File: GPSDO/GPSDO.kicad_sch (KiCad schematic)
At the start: 96 parts, among them IC4 AD8620, IC5 LD1117S12TR_SOT223, IC7 74HC14, IC9 MCP4725, J2 SolderJumper_3_Open, J3 SolderJumper_2_Open, K1 Conn_01x04, K10 Conn_01x03, K11 Conn_01x07, K12 SW_Push, K13 Conn_01x03, K14 Conn_01x05, K2 Conn_01x02, K3 Conn_01x02, K4 Conn_01x03, K5 Jumper_3_Open, K6 Conn_01x05, K7 Conn_01x02, K8 Conn_02x03_Odd_Even, K9 Conn_Coaxial, Q1 NPN

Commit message: changed schematic, OCXO symbol from Gibbi
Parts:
- removed C12: 1µ, symbol Device:C
- removed C15, C5: 100n, symbol Device:C
- removed C16: 1n, symbol Device:C
- removed D3: D, symbol Device:D
- removed F1: 1.6A, symbol Device:Fuse
- removed unit 1 of IC4
- removed IC5: LD1117S12TR_SOT223, Package_TO_SOT_SMD:SOT-223-3_TabPin2, symbol Regulator_Linear:LD1117S12TR_SOT223
- removed IC9: MCP4725, Package_TO_SOT_SMD:SOT-23-6, symbol Analog_DAC:MCP4725xxx-xCH
- removed OCXO1: ~, symbol GPSDO-Components:OCXO
- removed Q1: NPN, symbol Simulation_SPICE:NPN
- removed R14: 10k, symbol Device:R_Potentiometer
- removed R17, R18: 240, symbol Device:R
- removed R19, R20, R21: 2.4k, symbol Device:R
- removed RE1: G6K-2, symbol Relay:G6K-2
- removed TP3: Conn_01x01_Pin, symbol Connector:Conn_01x01_Pin
- added C5: 330n, symbol Device:C_Polarized
- added IC4: AD8620, Package_SO:SOIC-8_3.9x4.9mm_P1.27mm, symbol Amplifier_Operational:AD8620
- added J1: Conn_01x01_Pin, symbol Connector:Conn_01x01_Pin
- added OCXO2: ~, gibbi:OSC5A2B02, symbol GPSDO-Components:OSC5A2B02
- added SW1: SW_Nidec_CAS-120A1, Button_Switch_SMD:Nidec_Copal_CAS-120A, symbol Switch:SW_Nidec_CAS-120A1
- added U1: LM7805_TO220, Package_TO_SOT_THT:TO-220-3_Vertical, symbol Regulator_Linear:LM7805_TO220
- added U2: DAC8571IDGK, Package_SO:MSOP-8_3x3mm_P0.65mm, symbol Analog_DAC:DAC8571IDGK
- C13: value 470µ -> 100n
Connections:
- net GND: now also C5.2, OCXO2.2 (GND), U1.2 (GND), U2.5 (A0), U2.8 (GND)
- net VCC: now also SW1.2 (B)
- net at A1.23 (A4), K14.3 (Pin_3), K6.3 (Pin_3)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: now also U2.7 (SDA)
- net at A1.24 (A5), K14.4 (Pin_4), K6.4 (Pin_4)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: now also U2.6 (SCL)
- net at K7.2 (Pin_2): now also D1.2 (A)
- net at IC4.6 (-): no longer IC4.7
- net at C17.1, C19.1, L3.2: now also OCXO2.5 (VCC)
- net at IC7.1, R22.2, R23.1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: now also OCXO2.1 (10MHz)
- net at C11.2, R15.1: now also IC4.5 (+)
- net at D1.1 (K): now also C5.1, U1.1 (VI); no longer C13.1
- net at R16.1: now also IC4.6 (-), OCXO2.3 (Vcont); no longer A1.22 (A3)
- net at C14.1, L5.1: now also U2.1 (V_{DD}), U2.2 (V_{REF})
- net comp: now reaches A1.15 (D12)
- net comp: now also IC4.7
- net at R16.2: now also U2.3 (V_{SENSE}), U2.4 (V_{OUT})
- net V_ocxo: no longer names the net of A1.20 (A1)
- new net: C13.1, SW1.3 (A), U1.3 (VO)
- new net: J1.1 (Pin_1), SW1.1 (C)
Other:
- note added: "+5V"
- note added: "DC 7 - 25V"
- note removed: "DC 7.5 - 9V"
- note removed: "Manual Holdover"
- note removed: "V_Holdover"
- moved on the sheet: A1, C1, C10, C11, C14, C17, C18, C19, C2, C20, C21, C22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

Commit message: Add Frequency Multiplier and Pico
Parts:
- removed A1: Arduino_Nano_v3, Module:Arduino_Nano, symbol MCU_Module:Arduino_Nano_v3.x
- removed IC4: AD8620, Package_SO:SOIC-8_3.9x4.9mm_P1.27mm, symbol Amplifier_Operational:AD8620
- removed K10, K13, K4: Conn_01x03, symbol Connector_Generic:Conn_01x03
- removed K11: Conn_01x07, symbol Connector_Generic:Conn_01x07
- removed K14, K6: Conn_01x05, symbol Connector_Generic:Conn_01x05
- added C12, C16: 40p, symbol Device:C
- added C15, C23: 0.1u, symbol Device:C
- added J4, J5: SolderJumper_3_Open, symbol Jumper:SolderJumper_3_Open
- added K4, K6: Conn_Coaxial, symbol Connector:Conn_Coaxial
- added R14, R17, R19, R21: 10k, symbol Device:R
- added RV1: 2k, symbol Device:R_Potentiometer
- added RV2: 4k, symbol Device:R_Potentiometer
- added U3: Pico, RPi_Pico:RPi_Pico_SMD_TH, symbol MCU_RaspberryPi_and_Boards:Pico
- added U4, U6: TLV3501AID, Package_SO:SOIC-8_3.9x4.9mm_P1.27mm, symbol Comparator:TLV3501AID
- added U5: 74LVC2G86, symbol 74xGxx:74LVC2G86
- R8: value 2.4k -> 0
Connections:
- net GND: now also C12.1, C16.1, K4.2 (Ext), K6.2 (Ext), R17.2, R19.2, U3.13 (GND), U3.18 (GND), U3.23 (GND), U3.28 (GND), U3.38 (GND), U3.42 (GND), U3.8 (GND), U4.4 (V-), U5.4 (GND), U6.4 (V-)
- net VCC: now also C15.2, R14.1
- net comp: now also U3.29 (GPIO22)
- net at R8.2: now also RV2.1, U5.2
- net at C1.2, C7.1, C8.1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: now also IC1.1 (LD), U3.40 (VBUS); no longer R8.1
- net at K9.1 (In), R24.1, R25.1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: now also R8.1
- net at R12.1, U2.7 (SDA): now also U3.31 (GPIO26_ADC0)
- net at R13.1, U2.6 (SCL): now also U3.32 (GPIO27_ADC1)
- net at R5.1: now also U3.4 (GPIO2)
- net at R7.2: now also J4.1 (A), J5.3 (B)
- net at K1.3 (Pin_3): now also J4.3 (B), J5.1 (A)
- new net: R19.1, R21.2, U6.3 (+)
- new net: C16.2, RV1.2, U6.2 (-)
- new net: C12.2, RV2.2, U4.2 (-)
- new net: R14.2, R17.1, U4.3 (+)
- new net: U4.6, U5.1
- new net: C15.1, U4.7 (V+)
- new net: J4.2 (C), U3.2 (GPIO1)
- new net: C23.1, U6.7 (V+)
- new net: C23.2, R21.1
- new net: J5.2 (C), U3.1 (GPIO0)
- new net: K4.1 (In), U5.3
- new net: U5.5, U6.6
- new net: K6.1 (In), RV1.3, U5.6, U5.7
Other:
- note added: "10MHz out"
- note added: "20MHz out"
- note added: "3.3V or 5V?"
- note added: "40MHz out"
- note removed: "Forced Holdover"
- note removed: "SPI"
- note removed: "Temp Sensor"
- moved on the sheet: C1, C10, C11, C13, C14, C17, C18, C19, C2, C20, C21, C22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

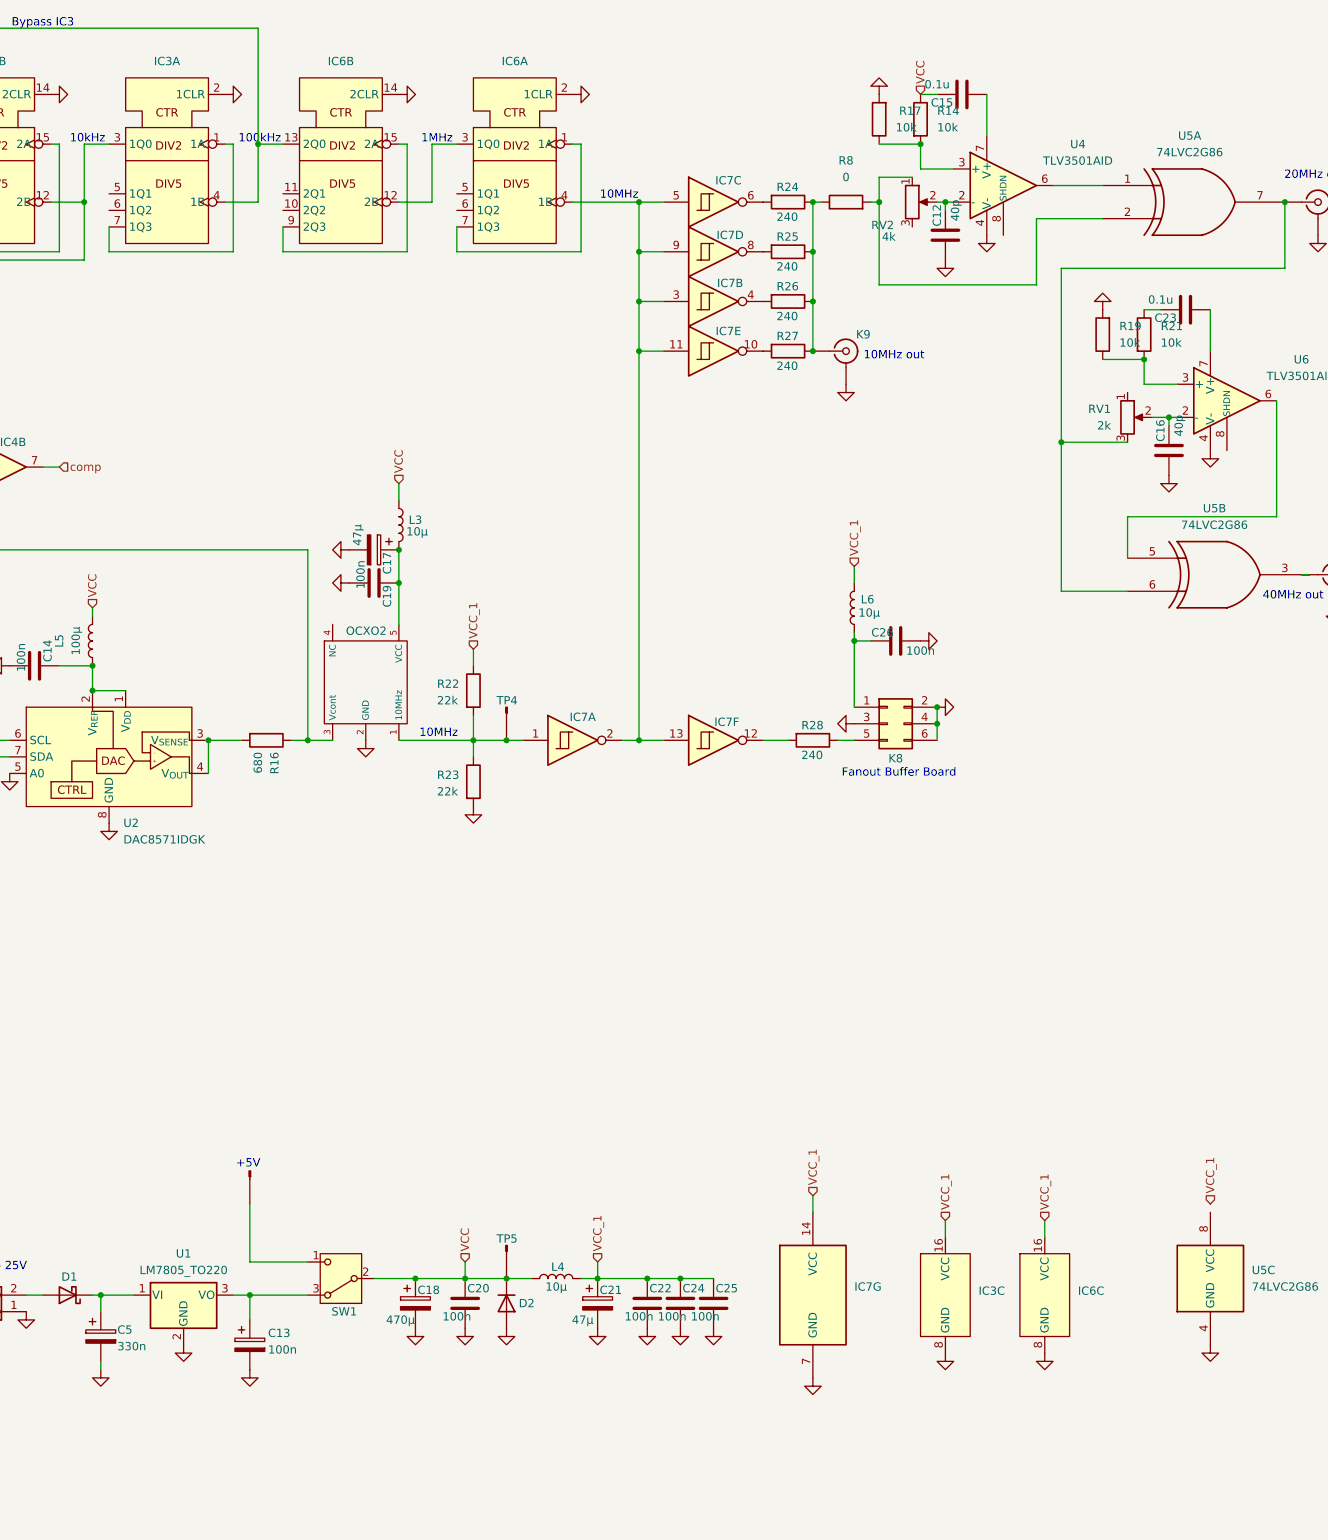
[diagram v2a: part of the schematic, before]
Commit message: minor schematic changes, added most footprints
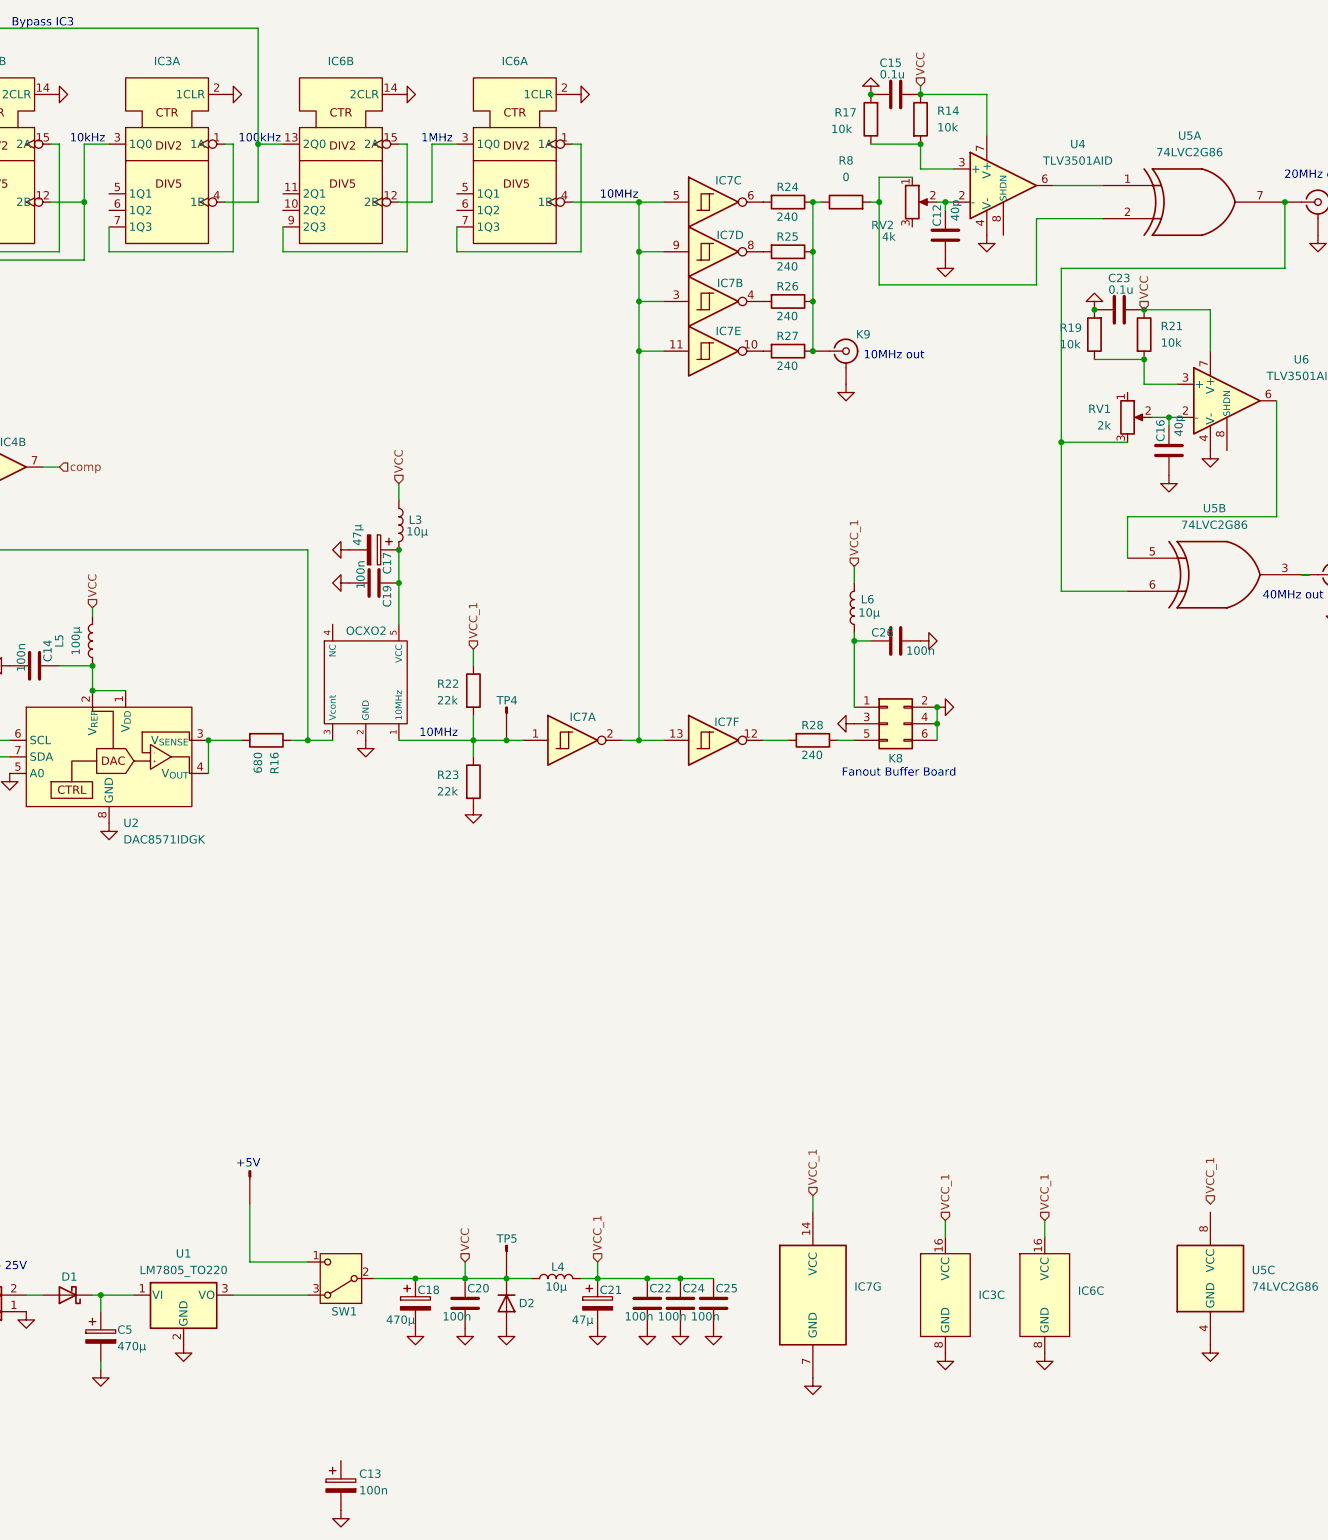
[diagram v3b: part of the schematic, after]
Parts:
- C1, C12, C14, C15, C16, C19, C20, C22, C23, C24, C25, C26, C4, C6, C8: footprint (none) -> Capacitor_SMD:C_1210_3225Metric_Pad1.33x2.70mm_HandSolder
- C10, C9: footprint (none) -> Capacitor_Tantalum_SMD:CP_EIA-7343-43_Kemet-X_Pad2.25x2.55mm_HandSolder
- C11, C3: footprint (none) -> Capacitor_THT:C_Rect_L7.2mm_W3.5mm_P5.00mm_FKS2_FKP2_MKS2_MKP2
- C17, C2, C21, C7: footprint (none) -> Capacitor_THT:CP_Radial_D6.3mm_P2.50mm
- C18: footprint (none) -> Capacitor_THT:CP_Radial_D10.0mm_P5.00mm
- C5: value 330n -> 470µ; footprint (none) -> Capacitor_THT:CP_Radial_D10.0mm_P5.00mm
- D1: footprint Diode_SMD:D_SMA -> Diode_SMD:D_SMA-SMB_Universal_Handsoldering
- D2: footprint (none) -> Diode_THT:D_DO-15_P10.16mm_Horizontal
- IC1, IC3, IC6: footprint (none) -> Package_SO:SOIC-16_3.9x9.9mm_P1.27mm
- J1, TP1, TP2, TP4, TP5: footprint (none) -> TestPoint:TestPoint_Pad_D1.0mm
- J2, J4, J5: footprint (none) -> Jumper:SolderJumper-3_P1.3mm_Open_RoundedPad1.0x1.5mm_NumberLabels
- J3: footprint (none) -> Jumper:SolderJumper-2_P1.3mm_Open_RoundedPad1.0x1.5mm
- K8: footprint (none) -> Connector_IDC:IDC-Header_2x03_P2.54mm_Vertical
- R1, R10, R11, R12, R13, R14, R15, R16, R17, R19, R2, R21, R22, R23, R24, R25, R26, R27, R28, R29, R3, R4, R5, R6, R7, R9: footprint (none) -> Resistor_SMD:R_1210_3225Metric_Pad1.30x2.65mm_HandSolder
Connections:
- net GND: now also C15.2, C23.2
- net VCC: now also C15.1, C23.1, R21.1, U4.7 (V+), U6.7 (V+); no longer C15.2
- net at SW1.3 (A), U1.3 (VO): no longer C13.1
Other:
- moved on the sheet: R17, R19

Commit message: added footprints and Mouser Links to components
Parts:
- removed C13: 100n, symbol Device:C_Polarized
- removed C23: 0.1u, Capacitor_SMD:C_1210_3225Metric_Pad1.33x2.70mm_HandSolder, symbol Device:C
- removed K2: Conn_01x02, symbol Connector_Generic:Conn_01x02
- removed R19, R21: 10k, Resistor_SMD:R_1210_3225Metric_Pad1.30x2.65mm_HandSolder, symbol Device:R
- removed U4, U6: TLV3501AID, Package_SO:SOIC-8_3.9x4.9mm_P1.27mm, symbol Comparator:TLV3501AID
- added IC2: ~, Package_TO_SOT_SMD:SOT-23-8_Handsoldering, symbol GPSDO-Components:TLV3502
- added K2: Conn_01x01_Pin, TestPoint:TestPoint_Loop_D2.50mm_Drill1.85mm, symbol Connector:Conn_01x01_Pin
- IC7: footprint (none) -> Package_SO:SOIC-14_3.9x8.7mm_P1.27mm
- K1: footprint (none) -> Connector_PinHeader_2.54mm:PinHeader_1x04_P2.54mm_Vertical
- K12, K3: footprint (none) -> Connector_PinHeader_2.54mm:PinHeader_1x02_P2.54mm_Vertical
- K4, K6, K9: footprint (none) -> Connector_Coaxial:SMA_Molex_73251-1153_EdgeMount_Horizontal
- K5: footprint (none) -> Connector_PinHeader_2.54mm:PinHeader_1x03_P2.54mm_Vertical
- K7: footprint (none) -> Connector_BarrelJack:BarrelJack_CUI_PJ-102AH_Horizontal
- L1, L5: footprint (none) -> Inductor_SMD:L_Neosid_SM-PIC0612H
- L2, L3, L4, L6: footprint (none) -> Inductor_SMD:L_Cenker_CKCS6045
- SW1: footprint Button_Switch_SMD:Nidec_Copal_CAS-120A -> Button_Switch_THT:SW_E-Switch_EG1271_SPDT
- U1: footprint Package_TO_SOT_THT:TO-220-3_Vertical -> Package_TO_SOT_SMD:SOT-223-3_TabPin2
- U2: footprint Package_SO:MSOP-8_3x3mm_P0.65mm -> Package_SO:VSSOP-8_3.0x3.0mm_P0.65mm
- U5: footprint (none) -> Package_SO:TSSOP-8_3x3mm_P0.65mm
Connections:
- net GND: now also IC2.5 (V-)
- net VCC: now also IC2.8 (V+)
- net at R2.2: now also K2.1 (Pin_1)
- net at C16.2, RV1.2: now also IC2.4 (-)
- net at C12.2, RV2.2: now also IC2.2 (-)
- net VCC/2: now reaches R14.2, R17.1
- net VCC/2: now also IC2.1 (+), IC2.3 (+)
- net at U5.1: now also IC2.7
- net at U5.5: now also IC2.6
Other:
- note added: "100uH https://www.mouser.de/ProductDetail/TDK/SPM7054VC-101M-D?qs=sGAEpiMZZMv126LJFLh8yz4JeXP9OGKgXN2nn20c%2F50%3D"
- note added: "10uH https://www.mouser.de/ProductDetail/Monolithic-Power-Systems-MPS/MPL-SE5040-100?qs=sGAEpiMZZMv126LJFLh8yyOx6Bzv8ule8YDMbIBSVtI%3D"
- note added: "2x Ripple Counter https://www.mouser.de/ProductDetail/Texas-Instruments/CD74HC390M96?qs=q81XD9WTF%252BLJAyVsZ7eHLQ%3D%3D"
- note added: "Barrel-Jack DC connector https://www.mouser.de/ProductDetail/CUI-Devices/PJ-102AH?qs=WyjlAZoYn50Yq4CrVLCXLw%3D%3D"
- note added: "DAC https://www.mouser.de/ProductDetail/Texas-Instruments/DAC8571IDGK?qs=vul0MlC%2Fa1dvtLPGKelkTg%3D%3D"
- note added: "Dual OpAmp https://www.mouser.de/ProductDetail/Microchip-Technology/MCP6002-I-SN?qs=cQYLKLPzRJlt69SDaZwGcA%3D%3D"
- note added: "For the Comparators, both https://www.mouser.de/ProductDetail/Texas-Instruments/TLV3502AIDCNR?qs=m96fseALk3UVf1AatLxFqQ%3D%3D or https://www.mouser.de/ProductDetail/Texas-Instruments/TLV3502AID?qs=m96fseALk3U4Ee5H4Lg7qw%3D%3D work"
- note added: "Hex-Schmitt-Trigger https://www.mouser.de/ProductDetail/Texas-Instruments/CD74AC14M96?qs=7KMwW2o1%252BmTMcy6XciEnlg%3D%3D"
- note added: "PLL https://www.mouser.de/ProductDetail/Texas-Instruments/CD74HC7046AMT?qs=gb35HGp1gQI6mJ4fH4yL3g%3D%3D"
- note added: "Voltage Regulator https://www.mouser.de/ProductDetail/Texas-Instruments/LM7805MPX-NOPB?qs=gO6GG99qvRCSwIVAoVKHPw%3D%3D"
- note added: "XOR gates: https://www.mouser.de/ProductDetail/Nexperia/74LVC2G86DP125?qs=me8TqzrmIYU4VUcP1CeUGw%3D%3D"

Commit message: Started Layout (WIP), minor schematic changes (3.3V supply to GPS neo module, removed voltage divider, since RPico Pins already provide 3.3V only)
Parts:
- removed IC4: AD8620, Package_SO:SOIC-8_3.9x4.9mm_P1.27mm, symbol Amplifier_Operational:AD8620
- removed J4, J5: SolderJumper_3_Open, Jumper:SolderJumper-3_P1.3mm_Open_RoundedPad1.0x1.5mm_NumberLabels, symbol Jumper:SolderJumper_3_Open
- removed K12: SW_Push, Connector_PinHeader_2.54mm:PinHeader_1x02_P2.54mm_Vertical, symbol Switch:SW_Push
- removed R3: 680, Resistor_SMD:R_1210_3225Metric_Pad1.30x2.65mm_HandSolder, symbol Device:R
- removed R7: 330, Resistor_SMD:R_1210_3225Metric_Pad1.30x2.65mm_HandSolder, symbol Device:R
- added C13: 100n, Capacitor_SMD:C_1210_3225Metric_Pad1.33x2.70mm_HandSolder, symbol Device:C
- added U4: AD8620, Package_SO:SOIC-8_3.9x4.9mm_P1.27mm, symbol Amplifier_Operational:AD8620
- OCXO2: footprint gibbi:OSC5A2B02 -> OCXO_example:OSC5A2B02
- R8: footprint (none) -> Resistor_SMD:R_1210_3225Metric_Pad1.30x2.65mm_HandSolder
- RV1, RV2: footprint (none) -> Potentiometer_THT:Potentiometer_Bourns_3266Y_Vertical
- U3: footprint RPi_Pico:RPi_Pico_SMD_TH -> MCU_RaspberryPi_and_Boards:RPi_Pico_SMD_TH
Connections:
- net GND: now also C1.2, U3.3 (GND), U3.33 (AGND), C13.2, U4.4 (V-); no longer C1.1
- net VCC: now also L1.2, L2.1; no longer L1.1
- net VCC_1: now also U5.8 (VCC)
- net comp: now also U4.7
- net at R6.1: now also L1.1; no longer L1.2
- net at C7.1, C8.1, IC1.1 (LD)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: no longer C1.2, K1.1 (Pin_1), R12.2, R13.2
- net at K1.2 (Pin_2): now also U3.1 (GPIO0)
- net at C11.2, R15.1: now also U4.5 (+)
- net at OCXO2.3 (Vcont), R16.1: now also U4.6 (-)
- net at C14.1, L5.1, U2.1 (V_{DD})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: now also C13.1, U4.8 (V+)
- net at U3.2 (GPIO1): now also K1.3 (Pin_3)
- net at U3.36 (3V3): now also C1.1, K1.1 (Pin_1), R12.2, R13.2
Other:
- note added: "RX"
- note added: "TX"
- note added: "Unused second OpAmp in package. Leave it here for the time being"
- note removed: "3.3V or 5V?"
- moved on the sheet: C1, L1
